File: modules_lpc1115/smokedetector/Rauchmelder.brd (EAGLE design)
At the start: 38 x 65 mm, 70 parts, among them IC1 BD9G101, IC2 LPC1115, Q1 BC856, Q3 BCP52, Q4 ASFL, T1 BC847C

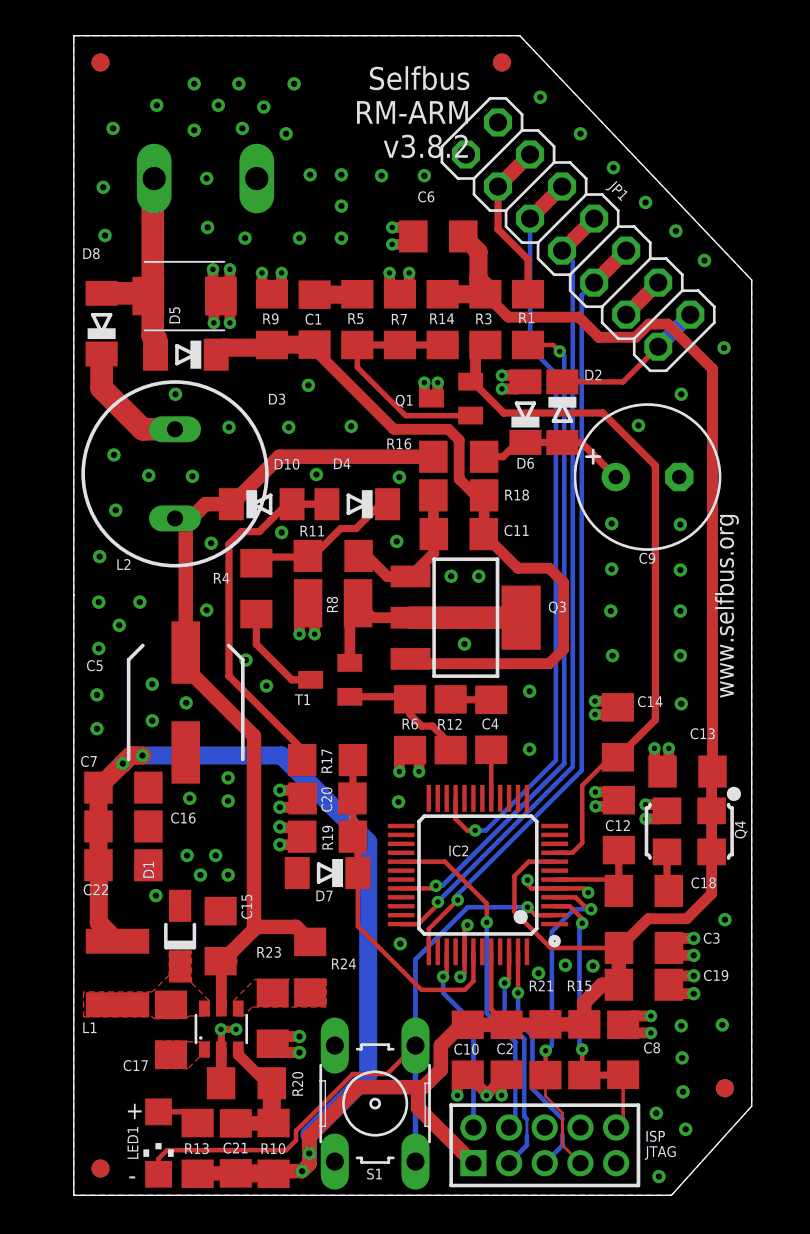
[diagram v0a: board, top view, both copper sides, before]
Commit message: [RM] - removed voltage divider again, added status LEDs, ...
- after a long discussion: we should use nowhere the voltage divider!
- status LEDs will help to identify problems when building the module
- optimized schematic
- added fiducials
- changed D1 to SMA footprint again
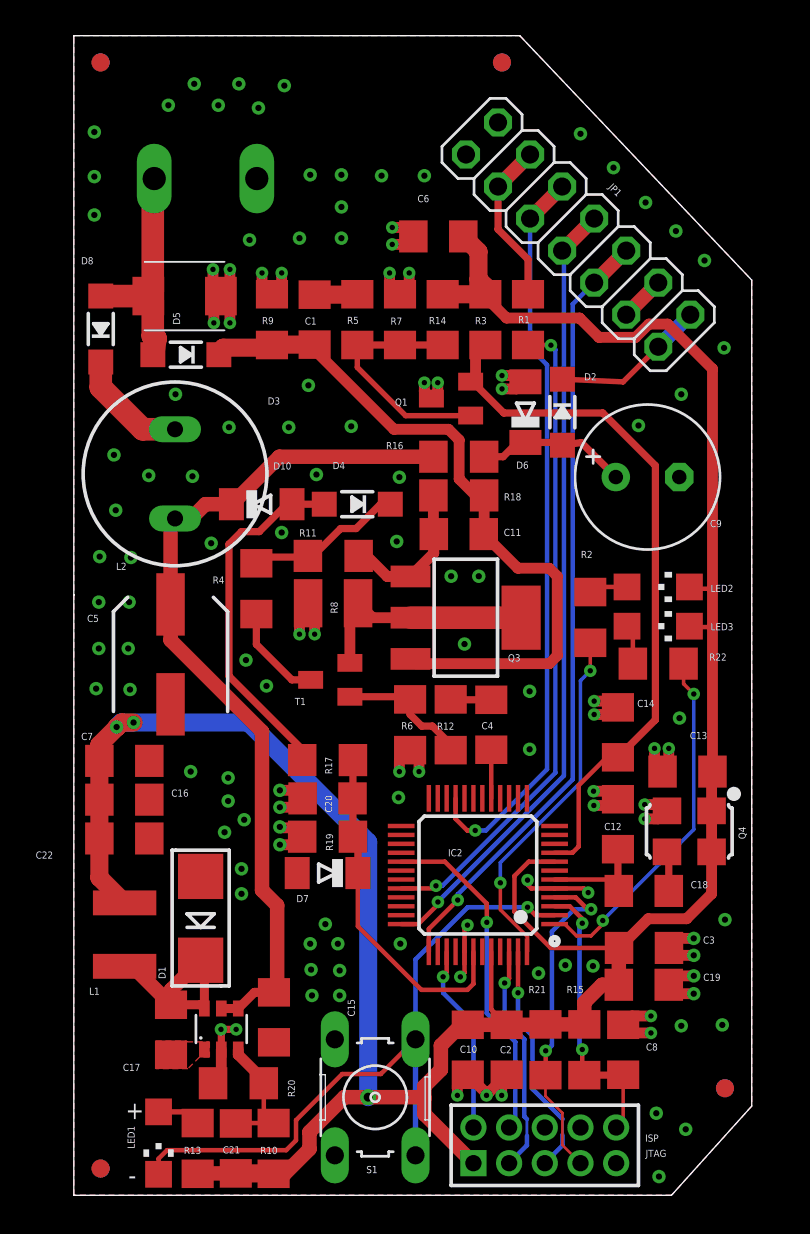
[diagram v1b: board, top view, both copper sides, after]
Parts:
- removed R23: 43k, rcl:R1206
- removed R24: 340k, rcl:R1206
- added LED2, LED3: (no value), led:CHIPLED_1206
- added R2, R22: 1k, rcl:R1206
- D1: device bt_diode:SOD123FL -> microbuilder:SMADIODE
- D2, D3, D4, D8: device diode:MINIMELF -> microbuilder:SOD-123
- moved C15 5.45 mm to (11.2, 9.97), turned to 90 degrees
- moved C5 2.83 mm to (5.42, 30.3)
- moved L1 2.19 mm to (2.85, 14.6)
- moved D1 1.52 mm to (7.11, 15.5)
- moved C16 1.50 mm to (2.83, 22.2)
- moved C22 1.50 mm to (2.83, 20.0)
- moved C7 1.50 mm to (2.83, 24.4)
- moved R20 0.45 mm to (9.23, 6.28)
- moved S1 0.35 mm to (16.9, 5.49)
- moved D8 0.30 mm to (1.51, 48.6)
- moved C12 0.07 mm to (30.5, 20.8)
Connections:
- removed net EN: IC1.4, R23.1, R24.2
- new net ARMINFO1: IC2.48, R2.1
- new net ARMINFO2: IC2.1, R22.1
- new net N$3: LED2.A, R2.2
- new net N$5: LED3.A, R22.2
- net +3V3: now also LED2.C, LED3.C
- net EIB_DC: now also IC1.4; no longer R24.1
- net GND: no longer R23.2
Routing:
- net ARMINFO2: track 0.00 -> 20.2 mm, vias 0 -> 2
- net ARMINFO1: track 0.00 -> 20.0 mm, vias 0 -> 2
- net LX: track 0.00 -> 11.4 mm
- net GND: track 77.6 -> 72.3 mm, vias 140 -> 125
- net +3V3: track 159.7 -> 156.2 mm, vias 4 -> 3
- net N$5: track 0.00 -> 2.24 mm
- net N$3: track 0.00 -> 2.18 mm
- net EIB_DC: track 50.3 -> 48.5 mm
- net N$26: track 14.6 -> 13.0 mm
- net LT8: track 37.2 -> 36.7 mm
- removed copper zone on layer 1, net EN
- removed copper zone on layer 1, net LX
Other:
- board text added: "Selfbus RM-ARM v3.8.3"
- board text removed: "Selfbus RM-ARM v3.8.2"

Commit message: [RM] Routed pwr suply switch / base detection
Merged olterions change with most recent verison
Routed addtional parts for base detection and pwr supply switch
Removed accidentially added v3.8.3
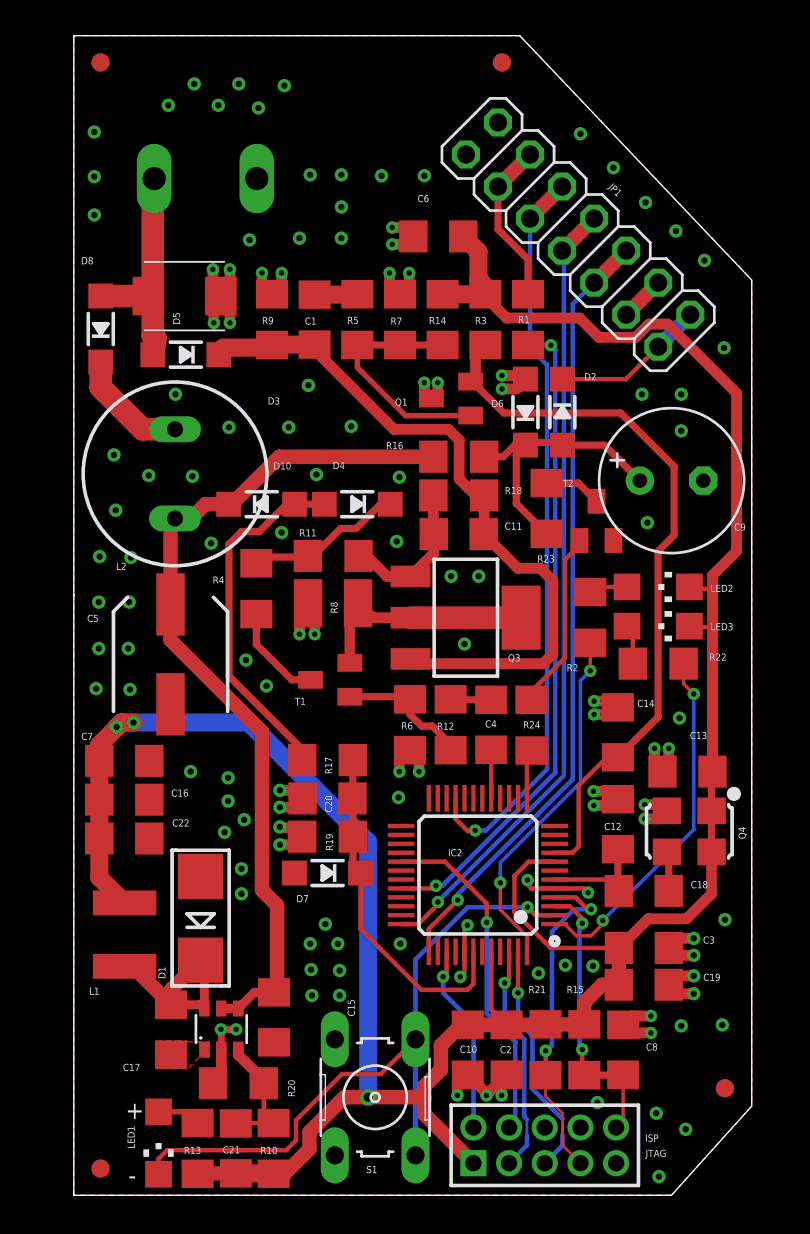
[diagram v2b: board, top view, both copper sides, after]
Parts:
- added R23: 120R, rcl:R1206
- added R24: 10k, rcl:R1206
- added T2: BC847C, transistor:SOT23
- D10, D6, D7: device diode:MINIMELF -> microbuilder:SOD-123
- moved C9 1.36 mm to (33.5, 40.1)
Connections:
- new net N$7: R23.2, T2.3
- new net N$8: R24.1, T2.1
- net GND: now also T2.2
- net LT1: now also R24.2
- net N$10: now also R23.1
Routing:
- net N$8: track 0.00 -> 10.0 mm
- net N$10: track 8.67 -> 16.0 mm
- net N$7: track 0.00 -> 3.22 mm
- net LT1: track 0.00 -> 2.78 mm
- net EIB_IN: track 39.7 -> 41.1 mm
- net +3V3: track 156.2 -> 157.3 mm
- net EIB+DIR: track 40.4 -> 39.7 mm
- net GND: track 72.3 -> 72.1 mm, vias 125 -> 126

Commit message: [RM] - pwr mlccs changed to 2 x 47uF and adj-voltage divider 1k6/470R
- according to ROHM spec: switched to 2 x 47uF mlccs (instead of 1 x 22uF of the old design)
- according to ROHM spec: adjusted voltage divider to get 3,3V output instead of  (instead of  3,397V from the old design)
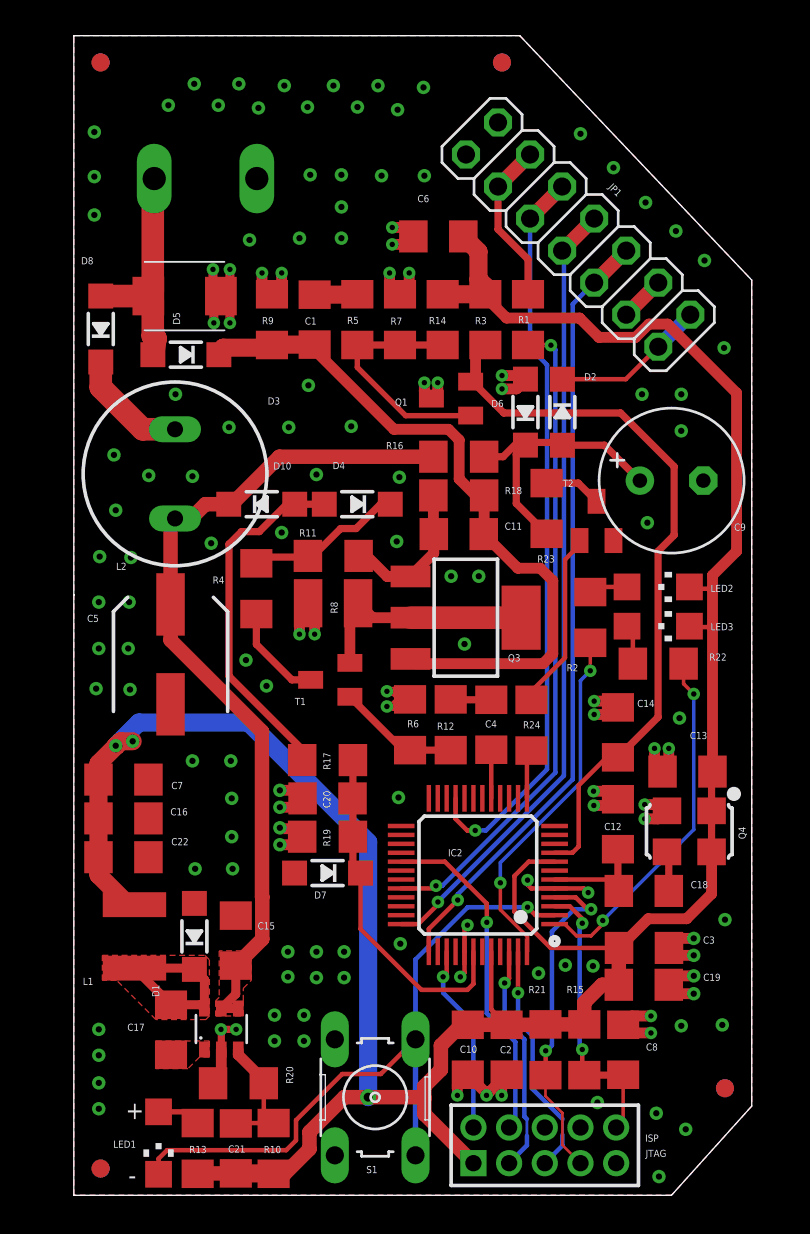
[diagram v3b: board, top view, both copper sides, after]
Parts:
- C16, C22: value 22µ/25V -> 47µ/10V
- D1: device microbuilder:SMADIODE -> microbuilder:SOD-123
- moved C15 4.80 mm to (9.08, 14.3), turned to 270 degrees
- moved D1 1.07 mm to (6.76, 14.5)
- moved C16 1.05 mm to (2.78, 21.1)
- moved C22 1.05 mm to (2.78, 18.9)
- moved C7 1.05 mm to (2.78, 23.3)
- moved L1 0.56 mm to (3.40, 14.5)
- turned R6 to 270 degrees
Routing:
- net GND: track 72.1 -> 74.6 mm, vias 126 -> 138
- net EIB_DC: track 48.5 -> 47.5 mm
- net LX: track 11.4 -> 10.7 mm
- net N$34: track 7.58 -> 6.89 mm
- added copper zone on layer 1, net EIB_DC
- added copper zone on layer 1, net LX

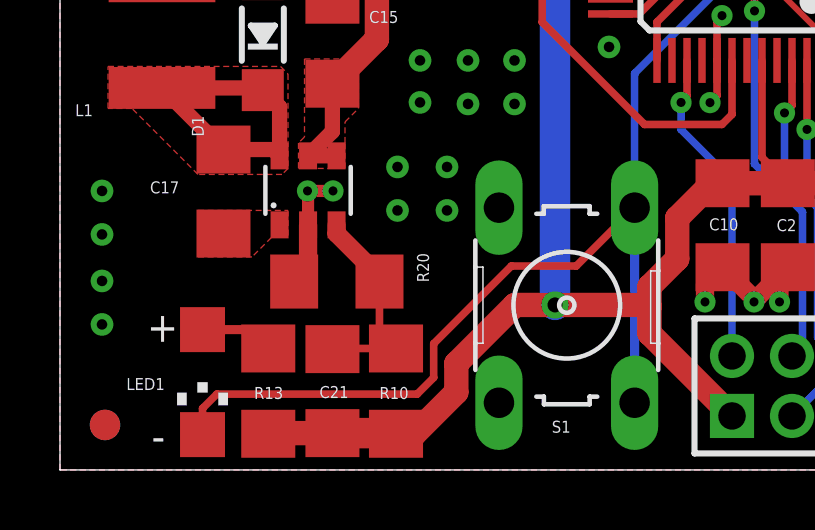
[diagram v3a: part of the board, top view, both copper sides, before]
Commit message: [RM] - removed thermals from buck converter polygons
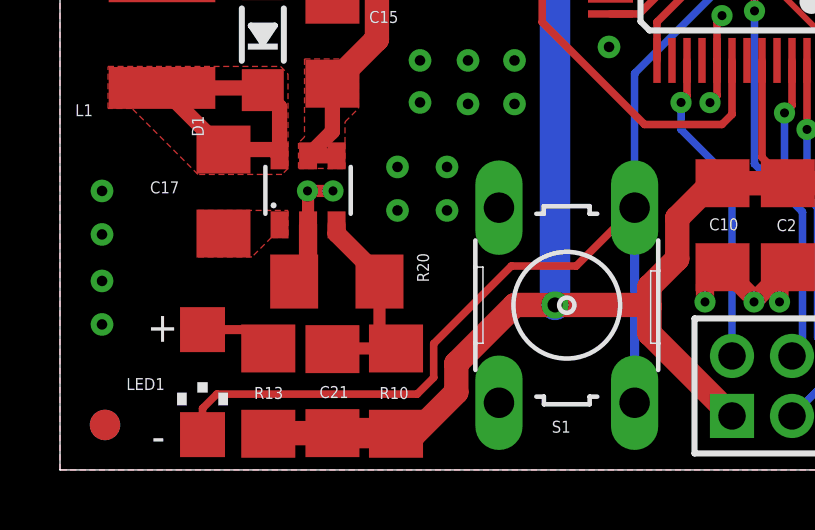
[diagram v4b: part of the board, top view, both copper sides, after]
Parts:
- R10: value 2k4 -> 1k6
- R20: value 680R -> 470R
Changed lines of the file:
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@@
 <attribute name="VALUE" x="3" y="8.359" size="0.4" layer="27"/>
 </element>
-<element name="R10" library="rcl" library_urn="urn:adsk.eagle:library:334" package="R1206" package3d_urn="urn:adsk.eagle:package:23540/2" value="2k4" x="11.2" y="2.6274125" smashed="yes" rot="R270">
+<element name="R10" library="rcl" library_urn="urn:adsk.eagle:library:334" package="R1206" package3d_urn="urn:adsk.eagle:package:23540/2" value="1k6" x="11.2" y="2.6274125" smashed="yes" rot="R270">
 <attribute name="NAME" x="10.64725" y="2.3646625" size="0.4" layer="25"/>
 <attribute name="POPULARITY" value="41" x="11.2" y="2.6274125" size="1.778" layer="27" rot="R270" display="off"/>
@@
 <attribute name="VALUE" x="12.94" y="3.1919125" size="0.4" layer="27" rot="R90"/>
 </element>
-<element name="R20" library="rcl" library_urn="urn:adsk.eagle:library:334" package="R1206" package3d_urn="urn:adsk.eagle:package:23540/2" value="680R" x="9.227" y="6.28" smashed="yes">
+<element name="R20" library="rcl" library_urn="urn:adsk.eagle:library:334" package="R1206" package3d_urn="urn:adsk.eagle:package:23540/2" value="470R" x="9.227" y="6.28" smashed="yes">
 <attribute name="NAME" x="12.3" y="6.257" size="0.4" layer="25" rot="R90"/>
 <attribute name="POPULARITY" value="41" x="9.227" y="6.28" size="1.778" layer="27" display="off"/>
@@
 <wire x1="10.5642" y1="14.35955" x2="9.08" y2="12.87535" width="0.8128" layer="1"/>
 <wire x1="10.55" y1="25.9925" x2="10.55" y2="16.73153125" width="0.8128" layer="1"/>
-<polygon width="0.0762" layer="1">
+<polygon width="0.0762" layer="1" thermals="no">
 <vertex x="8.15" y="13.7"/>
 <vertex x="8.15" y="11.1"/>
@@
 <wire x1="5.449" y1="10.68" x2="7.109" y2="10.68" width="0.508" layer="1"/>
 <wire x1="7.109" y1="10.68" x2="7.319" y2="10.47" width="0.508" layer="1"/>
-<polygon width="0.0762" layer="1">
+<polygon width="0.0762" layer="1" thermals="no">
 <vertex x="1.6" y="13.45"/>
 <vertex x="7.35" y="13.45"/>
@@
 <wire x1="10.649" y1="6.451" x2="10.649" y2="6.28" width="0.6096" layer="1"/>
 <wire x1="9.219" y1="7.881" x2="10.649" y2="6.451" width="0.6096" layer="1"/>
-<wire x1="10.649" y1="6.28" x2="10.649" y2="4.6004125" width="0.254" layer="1"/>
+<wire x1="10.649" y1="6.28" x2="10.649" y2="4.6004125" width="0.4064" layer="1"/>
 <wire x1="10.649" y1="4.6004125" x2="11.2" y2="4.0494125" width="0.254" layer="1"/>
 <wire x1="9.081" y1="4.0274125" x2="9.103" y2="4.0494125" width="0.254" layer="1"/>
-<wire x1="9.103" y1="4.0494125" x2="11.2" y2="4.0494125" width="0.254" layer="1"/>
+<wire x1="9.103" y1="4.0494125" x2="11.2" y2="4.0494125" width="0.4064" layer="1"/>
 </signal>
 <signal name="+3V3">

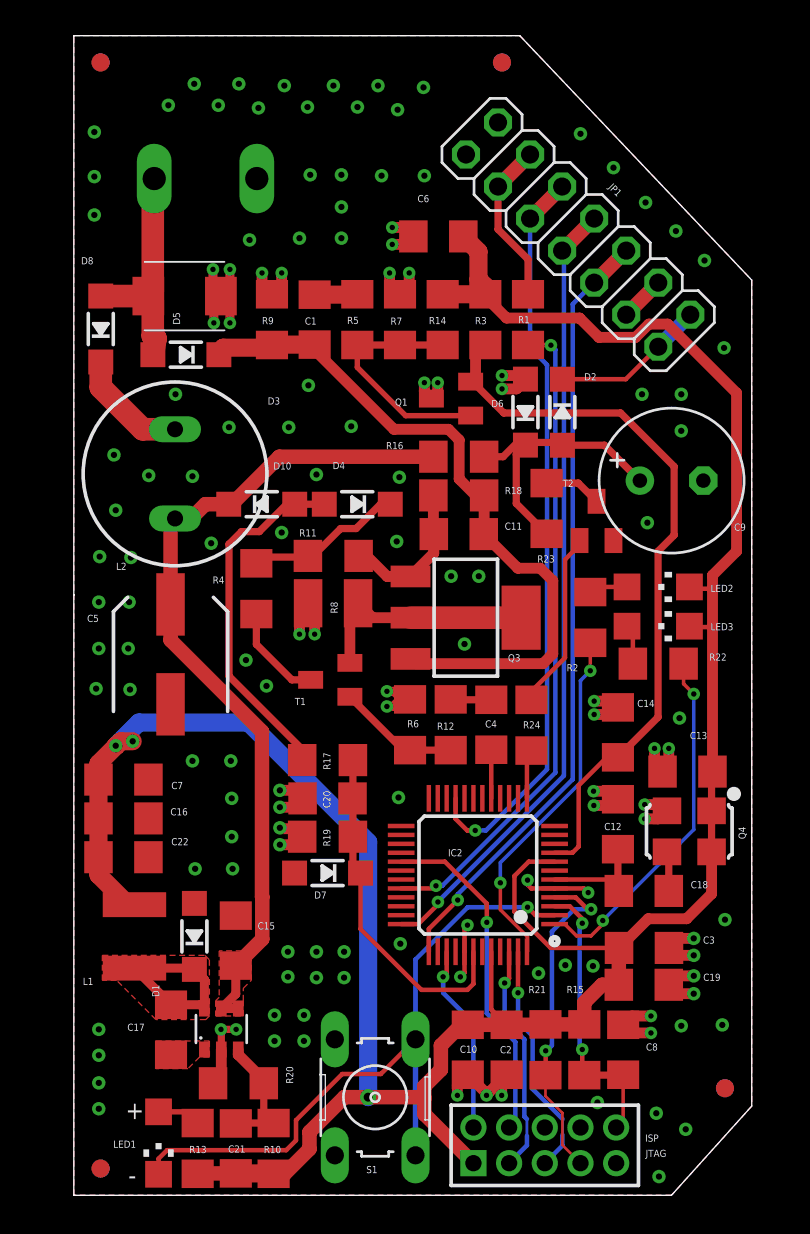
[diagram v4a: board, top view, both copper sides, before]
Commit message: [RM] - changed footprints from 1206 to 0805
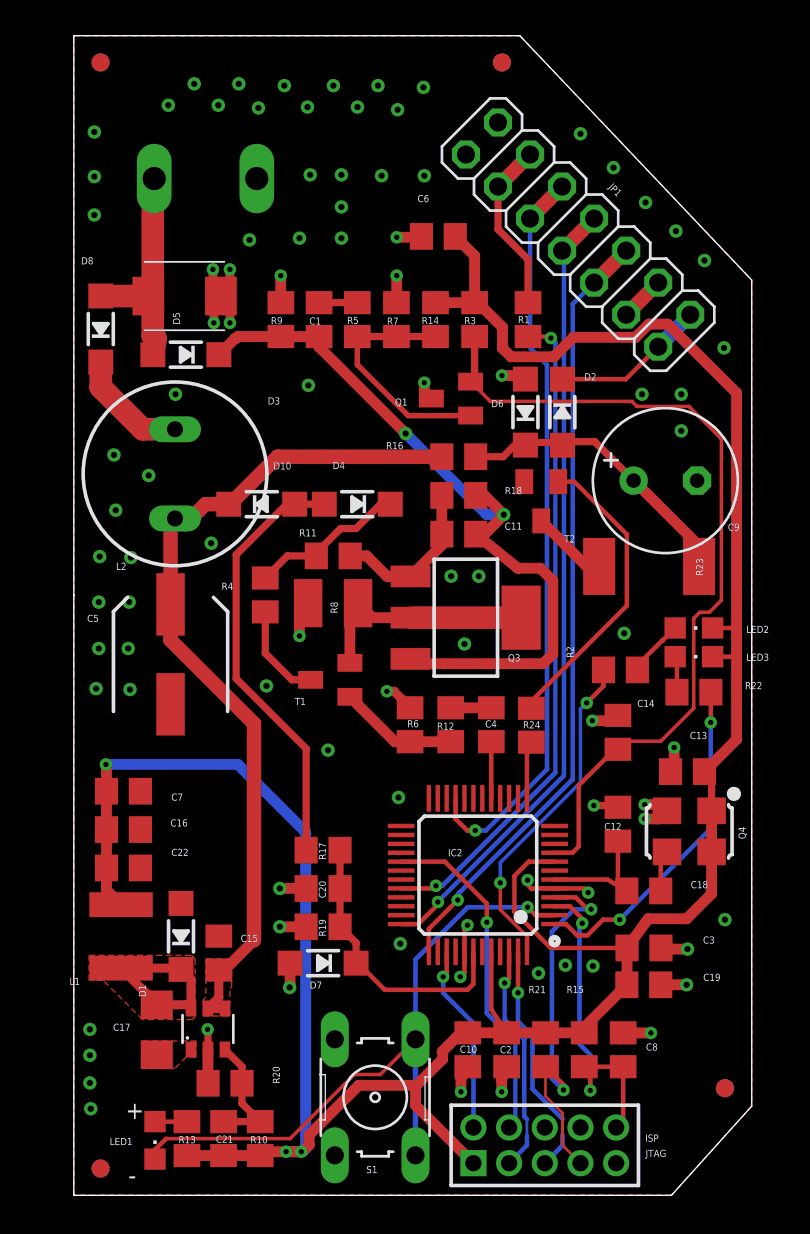
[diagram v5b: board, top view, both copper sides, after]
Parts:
- C1, C10, C3, C6, C7: value 100n -> 100nF; device rcl:C1206 -> rcl:C0805
- C11, C20, C8: device rcl:C1206 -> rcl:C0805
- C12: value 220p -> 220pF; device rcl:C1206 -> rcl:C0805
- C13, C4: value 10n -> 10nF; device rcl:C1206 -> rcl:C0805
- C14, C18: value 100p -> 100pF; device rcl:C1206 -> rcl:C0805
- C15: value 4.7µF/50V -> 4.7uF/50V; device rcl:C1206 -> rcl:C0805
- C16, C22: value 47µ/10V -> 47uF/10V; device rcl:C1206 -> rcl:C0805
- C19, C2: value 1µF -> 1uF; device rcl:C1206 -> rcl:C0805
- C21: value 270n -> 270nF; device rcl:C1206 -> rcl:C0805
- C5: value 100µ -> 100uF
- LED1, LED2, LED3: device led:CHIPLED_1206 -> led:CHIPLED_0805
- R1, R10, R11, R12, R13, R14, R15, R16, R17, R18, R19, R2, R20, R21, R22, R24, R3, R4, R5, R6, R7, R9: device rcl:R1206 -> rcl:R0805
- R23: value 120R -> 220R; device rcl:R1206 -> rcl:R2512
- moved R23 6.60 mm to (32.2, 35.2), turned to 180 degrees
- moved C20 5.06 mm to (14.0, 17.2)
- moved R17 5.06 mm to (14.0, 19.3)
- moved D7 5.06 mm to (14.0, 13.0)
- moved R19 5.06 mm to (14.0, 15.1)
- moved R2 3.39 mm to (30.6, 29.4), turned to 0 degrees
- moved T2 3.29 mm to (26.2, 38.9), turned to 180 degrees
- moved LED2 3.05 mm to (34.8, 31.8)
- moved LED3 2.63 mm to (34.8, 30.2)
- moved R22 2.56 mm to (34.8, 28.2)
- moved C15 1.18 mm to (8.13, 13.6)
- moved R10 0.93 mm to (10.4, 3.18)
- moved C21 0.88 mm to (8.40, 3.18)
- moved R13 0.81 mm to (6.34, 3.18)
- moved C17 0.80 mm to (4.65, 9.28)
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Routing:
- net GND: track 74.6 -> 48.9 mm, vias 138 -> 91
- net N$8: track 10.0 -> 17.0 mm
- net EIB_IN: track 41.1 -> 47.2 mm
- net REF: track 20.1 -> 24.3 mm
- net BUS_V1: track 19.3 -> 15.8 mm
- net ISP_EN: track 19.0 -> 22.1 mm
- net EIB+DIR: track 39.7 -> 42.6 mm, vias 0 -> 2
- net RESET: track 16.2 -> 19.0 mm
- net ARMINFO1: track 20.0 -> 18.8 mm
- net N$7: track 3.22 -> 4.31 mm
- net N$3: track 2.18 -> 3.24 mm
- net ARMINFO2: track 20.2 -> 19.1 mm
- net PROG: track 38.9 -> 37.9 mm
- net XTALIN: track 6.22 -> 7.22 mm
- net +3V3: track 157.3 -> 158.0 mm
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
